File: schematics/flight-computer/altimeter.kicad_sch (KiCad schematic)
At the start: 14 parts, among them U3 NVT2006BQ, U4 PCA9306, U5 ICM-20789, U6 MS5611-01BA

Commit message: Rename to Lychee
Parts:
- C13, C14, C15, C16: footprint Strix:C_0402 -> Lychee:C_0402
- R10, R5, R6, R7, R8, R9: footprint Strix:R_0402 -> Lychee:R_0402
- U3: footprint Strix:NVT2006BQ -> Lychee:NVT2006BQ
- U4: footprint Strix:PCA9306 -> Lychee:PCA9306
- U5: footprint Strix:ICM-20789 -> Lychee:ICM-20789
- U6: footprint Strix:MS5611-01BA -> Lychee:MS5611-01BA
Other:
- title: HAB Altimeter -> Lychee Flight Computer
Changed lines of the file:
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@@
   (paper "A4")
   (title_block
-    (title "HAB Altimeter")
-    (date "2021-08-31")
+    (title "Lychee Flight Computer")
+    (date "2021-12-31")
     (rev "1")
     (company "Cambridge University Spaceflight")
-    (comment 4 "Drawn By H. Franks")
+    (comment 1 "Drawn By H. Franks")
   )
   (junction (at 124.46 121.92) (diameter 0) (color 0 0 0 0)
@@
       (effects (font (size 1.27 1.27)) (justify left))
     )
-    (property "Footprint" "Strix:C_0402" (id 2) (at 72.39 82.55 0)
+    (property "Footprint" "Lychee:C_0402" (id 2) (at 72.39 82.55 0)
       (effects (font (size 1.27 1.27)) hide)
     )
@@
       (effects (font (size 1.27 1.27)) (justify right))
     )
-    (property "Footprint" "Strix:NVT2006BQ" (id 2) (at 87.63 65.405 0)
+    (property "Footprint" "Lychee:NVT2006BQ" (id 2) (at 87.63 65.405 0)
       (effects (font (size 1.27 1.27)) hide)
     )
@@
       (effects (font (size 1.27 1.27)) (justify left))
     )
-    (property "Footprint" "Strix:C_0402" (id 2) (at 93.98 132.08 0)
+    (property "Footprint" "Lychee:C_0402" (id 2) (at 93.98 132.08 0)
       (effects (font (size 1.27 1.27)) hide)
     )
@@
       (effects (font (size 1.27 1.27)) (justify left))
     )
-    (property "Footprint" "Strix:R_0402" (id 2) (at 127 114.3 0)
+    (property "Footprint" "Lychee:R_0402" (id 2) (at 127 114.3 0)
       (effects (font (size 1.27 1.27)) hide)
     )
@@
       (effects (font (size 1.27 1.27)) (justify left))
     )
-    (property "Footprint" "Strix:R_0402" (id 2) (at 124.46 114.3 0)
+    (property "Footprint" "Lychee:R_0402" (id 2) (at 124.46 114.3 0)
       (effects (font (size 1.27 1.27)) hide)
     )
@@
       (effects (font (size 1.27 1.27)) (justify left))
     )
-    (property "Footprint" "Strix:C_0402" (id 2) (at 62.23 82.55 0)
+    (property "Footprint" "Lychee:C_0402" (id 2) (at 62.23 82.55 0)
       (effects (font (size 1.27 1.27)) hide)
     )
@@
       (effects (font (size 1.27 1.27)) (justify left))
     )
-    (property "Footprint" "Strix:ICM-20789" (id 2) (at 124.46 92.71 0)
+    (property "Footprint" "Lychee:ICM-20789" (id 2) (at 124.46 92.71 0)
       (effects (font (size 1.27 1.27)) hide)
     )
@@
       (effects (font (size 1.27 1.27)) (justify left))
     )
-    (property "Footprint" "Strix:R_0402" (id 2) (at 71.12 114.3 0)
+    (property "Footprint" "Lychee:R_0402" (id 2) (at 71.12 114.3 0)
       (effects (font (size 1.27 1.27)) hide)
     )
@@
       (effects (font (size 1.27 1.27)) (justify left))
     )
-    (property "Footprint" "Strix:R_0402" (id 2) (at 72.39 72.39 0)
+    (property "Footprint" "Lychee:R_0402" (id 2) (at 72.39 72.39 0)
       (effects (font (size 1.27 1.27)) hide)
     )
@@
       (effects (font (size 1.27 1.27)) (justify left))
     )
-    (property "Footprint" "Strix:R_0402" (id 2) (at 73.66 114.3 0)
+    (property "Footprint" "Lychee:R_0402" (id 2) (at 73.66 114.3 0)
       (effects (font (size 1.27 1.27)) hide)
     )
@@
       (effects (font (size 1.27 1.27)) (justify right))
     )
-    (property "Footprint" "Strix:PCA9306" (id 2) (at 116.84 113.03 0)
+    (property "Footprint" "Lychee:PCA9306" (id 2) (at 116.84 113.03 0)
       (effects (font (size 1.27 1.27)) hide)
     )
@@
       (effects (font (size 1.27 1.27)) (justify left))
     )
-    (property "Footprint" "Strix:R_0402" (id 2) (at 93.98 114.3 0)
+    (property "Footprint" "Lychee:R_0402" (id 2) (at 93.98 114.3 0)
       (effects (font (size 1.27 1.27)) hide)
     )
@@
       (effects (font (size 1.27 1.27)) (justify left))
     )
-    (property "Footprint" "Strix:MS5611-01BA" (id 2) (at 196.85 115.57 0)
+    (property "Footprint" "Lychee:MS5611-01BA" (id 2) (at 196.85 115.57 0)
       (effects (font (size 1.27 1.27)) hide)
     )
@@
       (effects (font (size 1.27 1.27)) (justify left))
     )
-    (property "Footprint" "Strix:C_0402" (id 2) (at 83.82 132.08 0)
-      (effects (font (size 1.27 1.27)) hide)
-    )
+    (property "Footprint" "Lychee:C_0402" (id 2) (at 83.82 132.08 0)
+      (effects (font (size 1.27 1.27)) hide)
+    )

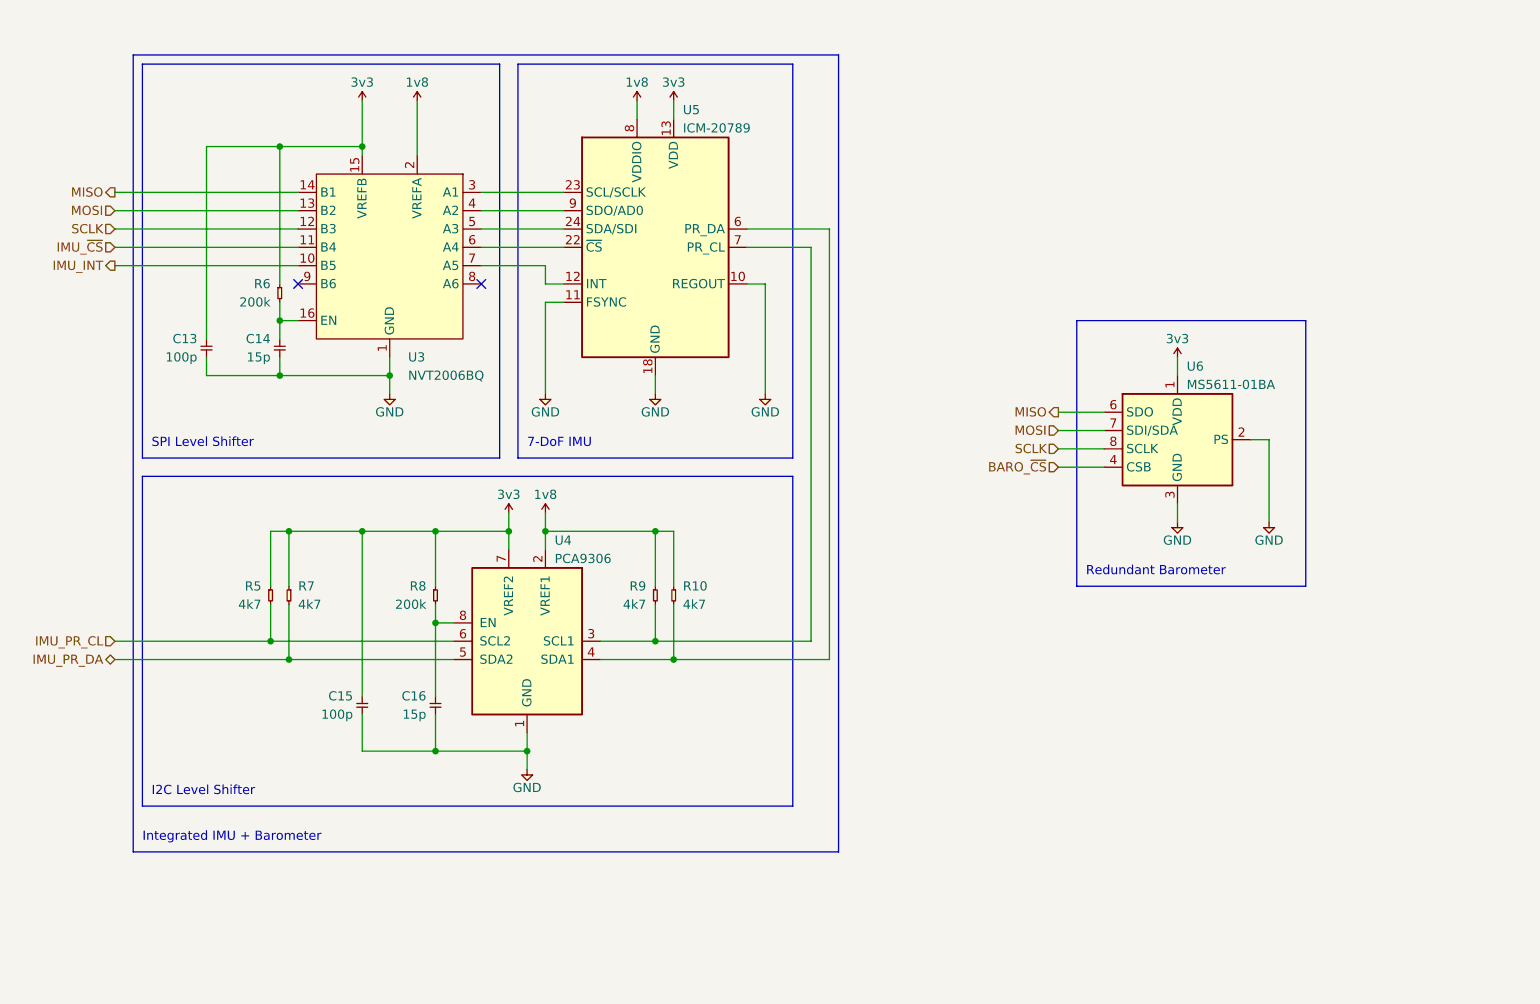
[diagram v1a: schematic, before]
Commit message: Migrate to common Strix lib via submodule
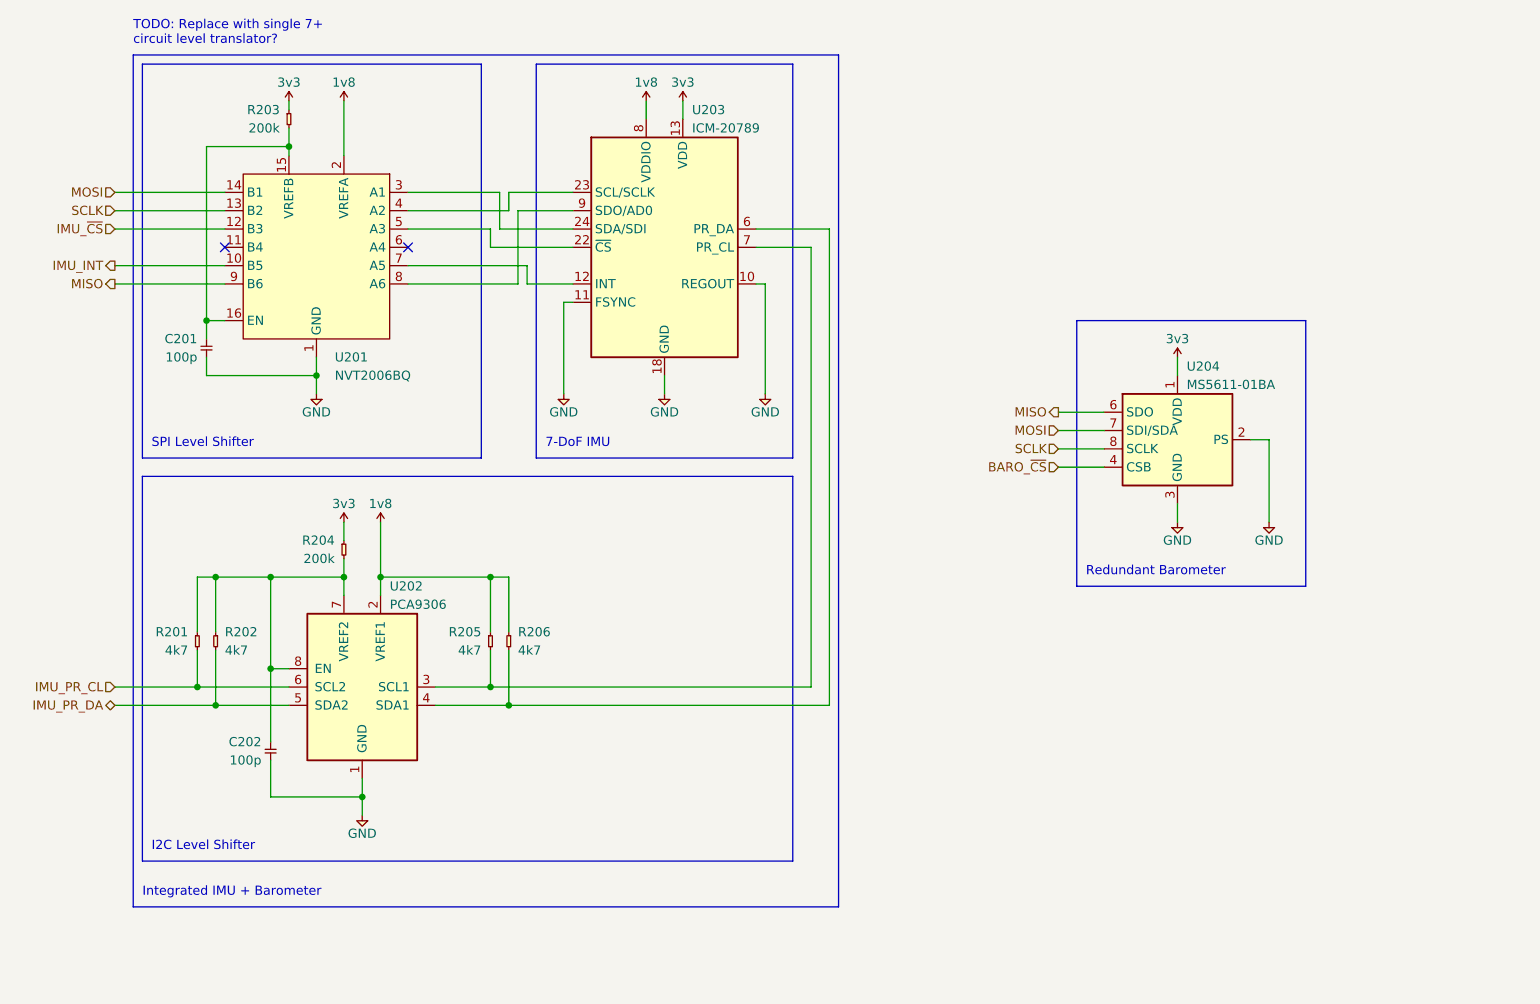
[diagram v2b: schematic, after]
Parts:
- removed C14, C16: 15p, Lychee:C_0402, symbol Strix:C
- C201: renamed from C13; footprint Lychee:C_0402 -> Strix:C_0402
- C202: renamed from C15; footprint Lychee:C_0402 -> Strix:C_0402
- R201: renamed from R5; footprint Lychee:R_0402 -> Strix:R_0402
- R202: renamed from R7; footprint Lychee:R_0402 -> Strix:R_0402
- R203: renamed from R6; footprint Lychee:R_0402 -> Strix:R_0402
- R204: renamed from R8; footprint Lychee:R_0402 -> Strix:R_0402
- R205: renamed from R9; footprint Lychee:R_0402 -> Strix:R_0402
- R206: renamed from R10; footprint Lychee:R_0402 -> Strix:R_0402
- U201: renamed from U3; footprint Lychee:NVT2006BQ -> Strix:NVT2006BQ
- U202: renamed from U4; footprint Lychee:PCA9306 -> Strix:PCA9306
- U203: renamed from U5; footprint Lychee:ICM-20789 -> Strix:ICM-20789
- U204: renamed from U6; footprint Lychee:MS5611-01BA -> Strix:MS5611-01BA
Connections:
- net 3v3: no longer C201.2, C202.2, R201.1, R202.1, U201.15 (VREFB), U202.7 (VREF2)
- net IMU_~{CS}: now also U201.12 (B3); no longer U201.11 (B4)
- net MISO: now also U201.9 (B6); no longer U201.14 (B1)
- net MOSI: now also U201.14 (B1); no longer U201.13 (B2)
- net SCLK: now also U201.13 (B2); no longer U201.12 (B3)
- net at R203.2, U201.16 (EN): now also C201.2, U201.15 (VREFB)
- net at U201.3 (A1): now also U203.24 (SDA/SDI); no longer U203.23 (SCL/SCLK)
- net at U201.4 (A2): now also U203.23 (SCL/SCLK); no longer U203.9 (SDO/AD0)
- net at U201.5 (A3): now also U203.22 (~{CS}); no longer U203.24 (SDA/SDI)
- net at U201.6 (A4): no longer U203.22 (~{CS})
- net at U201.8 (A6): now also U203.9 (SDO/AD0)
- net at R204.2, U202.8 (EN): now also C202.2, R201.1, R202.1, U202.7 (VREF2)
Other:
- note added: "TODO: Replace with single 7+ circuit level translator?"
- moved on the sheet: C202, R201, R202, R203, R204, R205, R206, U201, U202, U203

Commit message: Change level shifter to open drain compliant chip
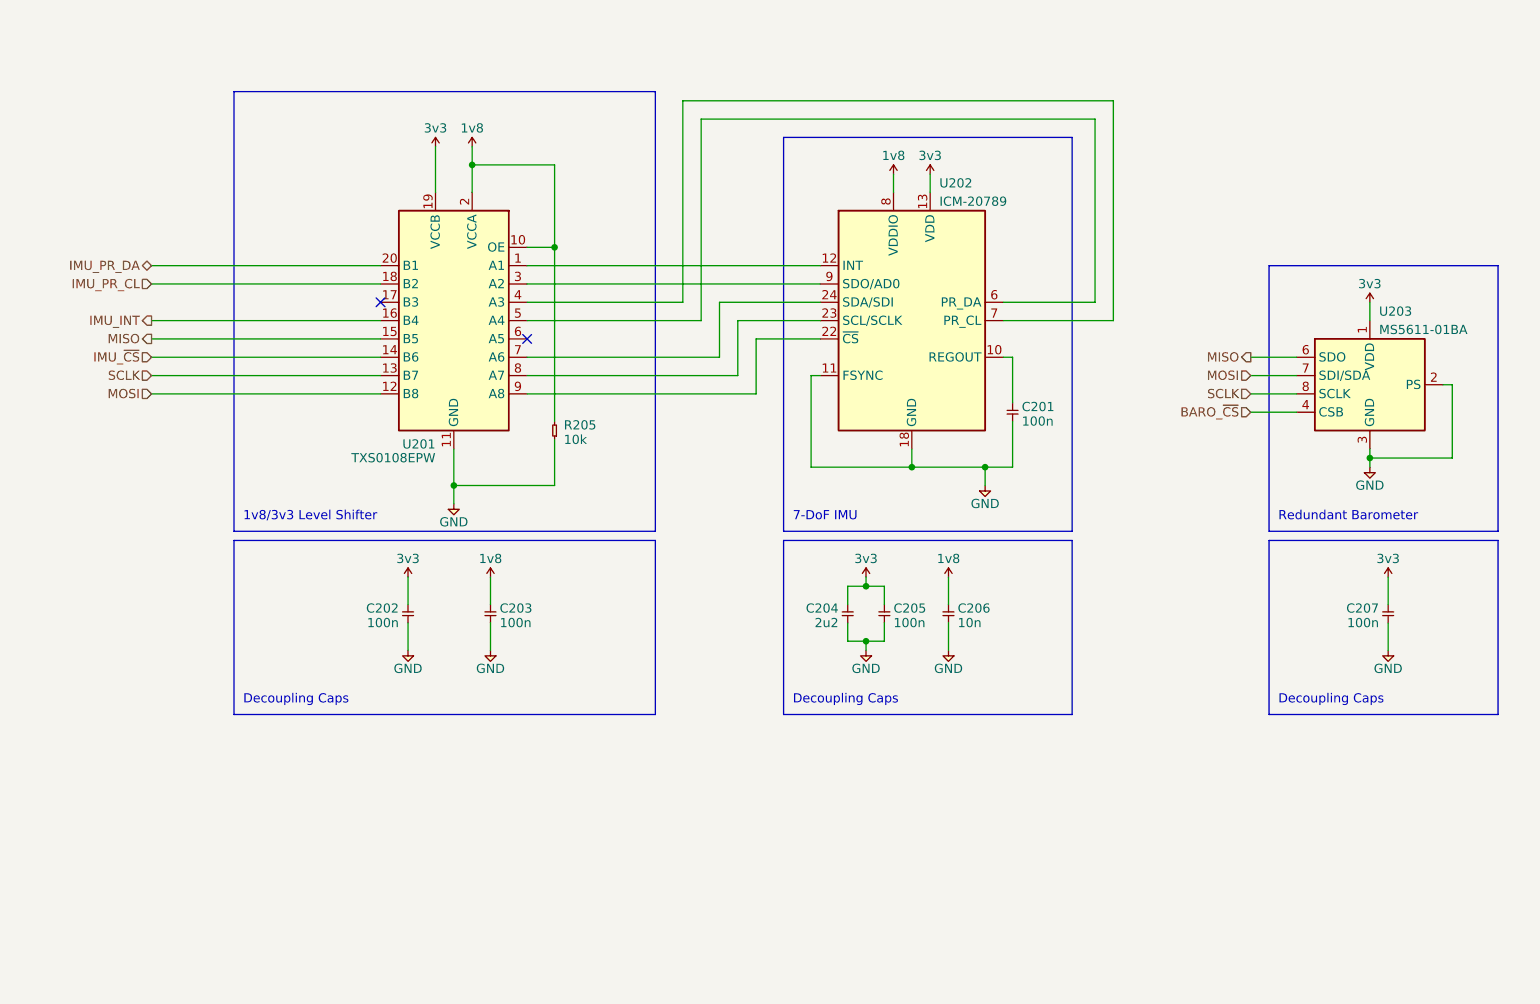
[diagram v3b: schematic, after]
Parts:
- removed R201, R202, R206: 4k7, Strix:R_0402, symbol Strix:R
- removed R203, R204: 200k, Strix:R_0402, symbol Strix:R
- removed U201: NVT2006BQ, Strix:NVT2006BQ, symbol Strix:NVT2006BQ
- removed U202: PCA9306, Strix:PCA9306, symbol Strix:PCA9306
- added C203, C205, C207: 100n, Strix:C_0402, symbol Strix:C
- added C204: 2u2, Strix:C_0402, symbol Strix:C
- added C206: 10n, Strix:C_0402, symbol Strix:C
- added U201: TXS0108EPW, Strix:TXS0108EPW, symbol Strix:TXS0108EPW
- C201, C202: value 100p -> 100n
- R205: value 4k7 -> 10k
- renumbered U203 to U202, U204 to U203
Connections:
- net 1v8: now also R205.2, C203.2, C206.2, U201.10 (OE), U201.2 (VCCA); no longer R205.1
- net 3v3: now also C202.2, C204.2, C205.2, C207.2, U201.19 (VCCB)
- net GND: now also R205.1, C203.1, C204.1, C205.1, C206.1, C207.1, U201.11 (GND); no longer U202.10 (REGOUT)
- net IMU_INT: now also U201.16 (B4)
- net IMU_PR_CL: now also U201.18 (B2)
- net IMU_PR_DA: now also U201.20 (B1)
- net IMU_~{CS}: now also U201.14 (B6)
- net MISO: now also U201.15 (B5)
- net MOSI: now also U201.12 (B8)
- net SCLK: now also U201.13 (B7)
- net at C201.2: now also U202.10 (REGOUT)
- net at U202.24 (SDA/SDI): now also U201.7 (A6)
- net at U202.23 (SCL/SCLK): now also U201.8 (A7)
- net at U202.22 (~{CS}): now also U201.9 (A8)
- net at U202.12 (INT): now also U201.1 (A1)
- net at U202.9 (SDO/AD0): now also U201.3 (A2)
- net at U202.6 (PR_DA): now also U201.5 (A4)
- net at U202.7 (PR_CL): now also U201.4 (A3); no longer R205.2
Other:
- note added: "1v8/3v3 Level Shifter"
- note added: "Decoupling Caps"
- note removed: "I2C Level Shifter"
- note removed: "Integrated IMU + Barometer"
- note removed: "SPI Level Shifter"
- note removed: "TODO: Replace with single 7+ circuit level translator?"
- moved on the sheet: U202, U203

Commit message: Complete first draft
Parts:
- removed U201: TXS0108EPW, Strix:TXS0108EPW, symbol Strix:TXS0108EPW
- added C203: 100n, Strix:C_0402, symbol Strix:C
- added R201: 200k, Strix:R_0402, symbol Strix:R
- added R202, R203, R204: 4k7, Strix:R_0402, symbol Strix:R
- added U201: NXB0108PW-Q100J, Strix:NXB0108PW-Q100J, symbol Strix:NXB0108PW-Q100J
- added U204: PCA9306, Strix:PCA9306, symbol Strix:PCA9306
- C201, C205, C207: Farnell (none) -> 9402047
- C204: Farnell (none) -> 2672111
- C206: Farnell (none) -> 1758924
- R205: value 10k -> 4k7
- renumbered C203 to C208
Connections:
- net 1v8: now also C203.2, R204.2, U201.10 (OE), U201.2 (VCC(A)), U204.2 (VREF1); no longer C208.2
- net 3v3: now also R201.2, R202.2, R203.2, U201.19 (VCC(B))
- net GND: now also C203.1, U201.11 (GND), U204.1 (GND); no longer R205.1
- net IMU_INT: now also U201.12 (B8)
- net IMU_PR_CL: now also R202.1, U204.6 (SCL2)
- net IMU_PR_DA: now also R203.1, U204.5 (SDA2)
- net IMU_~{CS}: now also U201.14 (B6)
- net MISO: now also U201.16 (B4)
- net MOSI: now also U201.15 (B5)
- net SCLK: now also U201.17 (B3)
- net at U202.12 (INT): now also U201.9 (A8)
- net at U202.22 (~{CS}): now also U201.7 (A6)
- net at U202.23 (SCL/SCLK): now also U201.4 (A3)
- net at U202.24 (SDA/SDI): now also U201.6 (A5)
- net SDA_1v8: now reaches U202.6 (PR_DA)
- net SDA_1v8: now also R204.1, U204.4 (SDA1)
- net SCL_1v8: now reaches U202.7 (PR_CL)
- net SCL_1v8: now also R205.1, U204.3 (SCL1)
- net at U202.9 (SDO/AD0): now also U201.5 (A4)
- new net: C208.2, R201.1, U204.7 (VREF2), U204.8 (EN)
- no-connect marks 2 -> 6
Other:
- note added: "I2C Level Shifter"
- note added: "SPI & GPIO Level Shifter"
- note removed: "1v8/3v3 Level Shifter"
- moved on the sheet: C201, C204, C205, C206, C207, C208, U202, U203
